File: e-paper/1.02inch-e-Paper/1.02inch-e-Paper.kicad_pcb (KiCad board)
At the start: 2 copper layers, 70 x 20.9 mm, 23 parts

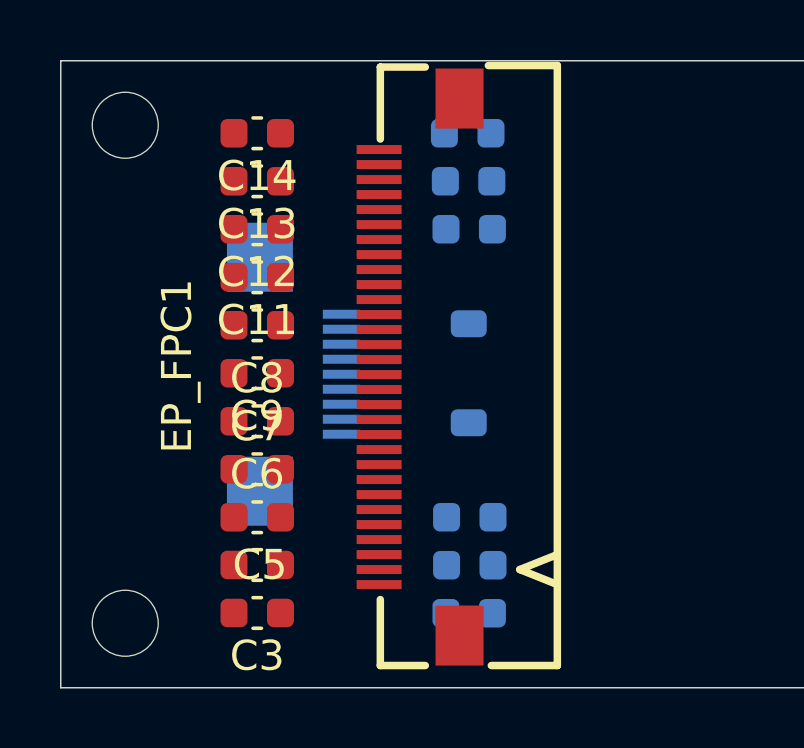
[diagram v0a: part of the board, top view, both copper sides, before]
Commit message: use 10pin connector socket instead of 9
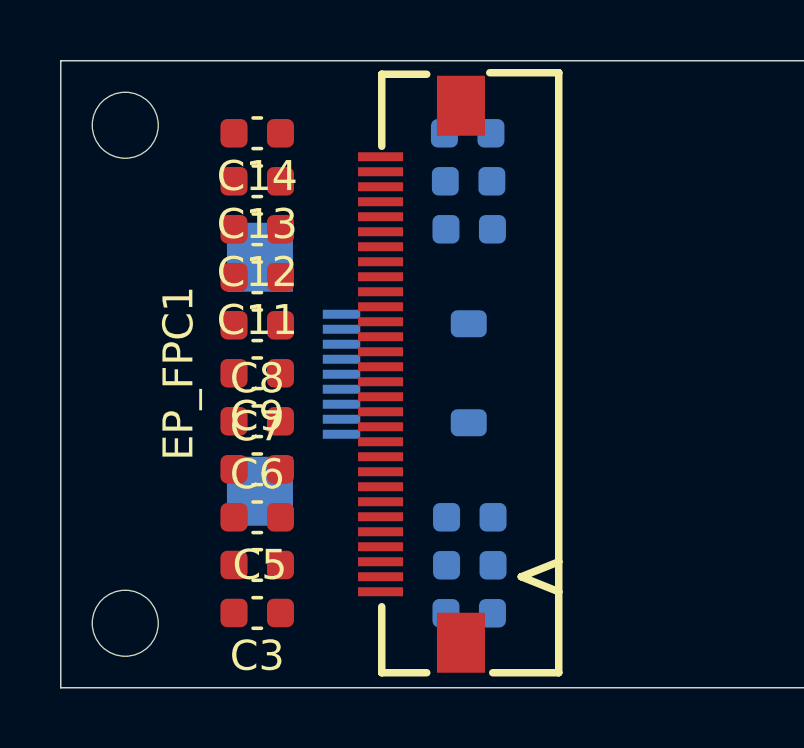
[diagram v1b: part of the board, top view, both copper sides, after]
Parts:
- moved EP_FPC1 0.24 mm to (12.0, 0.00)
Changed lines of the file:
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@@
 			)
 		)
-		(property "Datasheet" "~"
+		(property "Datasheet" ""
 			(at 0 0 0)
 			(layer "F.Fab")
@@
 			)
 		)
-		(property "Datasheet" "~"
+		(property "Datasheet" ""
 			(at 0 0 0)
 			(layer "F.Fab")
@@
 			)
 		)
-		(property "Datasheet" "~"
+		(property "Datasheet" ""
 			(at 0 0 0)
 			(layer "F.Fab")
@@
 			)
 		)
-		(property "Datasheet" "~"
+		(property "Datasheet" ""
 			(at 0 0 0)
 			(layer "F.Fab")
@@
 			)
 		)
-		(property "Datasheet" "~"
+		(property "Datasheet" ""
 			(at 0 0 0)
 			(layer "F.Fab")
@@
 			)
 		)
-		(property "Datasheet" "~"
+		(property "Datasheet" ""
 			(at 0 0 0)
 			(layer "F.Fab")
@@
 			)
 		)
-		(property "Datasheet" "~"
+		(property "Datasheet" ""
 			(at 0 0 0)
 			(layer "F.Fab")
@@
 			)
 		)
-		(property "Datasheet" "~"
+		(property "Datasheet" ""
 			(at 0 0 0)
 			(layer "F.Fab")
@@
 			)
 		)
-		(property "Datasheet" "~"
+		(property "Datasheet" ""
 			(at 0 0 0)
 			(layer "F.Fab")
@@
 	(footprint "ErgoCai.pretty:FPC-SMD_AFC01-S30FCA-00"
 		(layer "F.Cu")
-		(at 11.9525 -0.24 90)
+		(at 12 0 90)
 		(property "Reference" "EP_FPC1"
 			(at 0.0325 -8.075 90)
@@
 			)
 		)
-		(property "Datasheet" "~"
+		(property "Datasheet" ""
 			(at 0 0 0)
 			(layer "F.Fab")
@@
 			)
 		)
-		(property "Datasheet" "~"
+		(property "Datasheet" ""
 			(at 0 0 0)
 			(layer "F.Fab")
@@
 			)
 		)
-		(property "Datasheet" "~"
+		(property "Datasheet" ""
 			(at 0 0 0)
 			(layer "B.Fab")
@@
 			)
 		)
-		(property "Datasheet" "~"
+		(property "Datasheet" ""
 			(at 0 0 0)
 			(layer "B.Fab")
@@
 			)
 		)
-		(property "Datasheet" "~"
+		(property "Datasheet" ""
 			(at 0 0 270)
 			(unlocked yes)
@@
 			)
 		)
-		(property "Datasheet" "~"
+		(property "Datasheet" ""
 			(at 0 0 0)
 			(layer "B.Fab")
@@
 			)
 		)
-		(property "Datasheet" "~"
+		(property "Datasheet" ""
 			(at 0 0 0)
 			(layer "B.Fab")
@@
 			)
 		)
-		(property "Datasheet" "~"
+		(property "Datasheet" ""
 			(at 0 0 0)
 			(layer "B.Fab")
@@
 			)
 		)
-		(property "Datasheet" "~"
+		(property "Datasheet" ""
 			(at 0 0 180)
 			(layer "B.Fab")

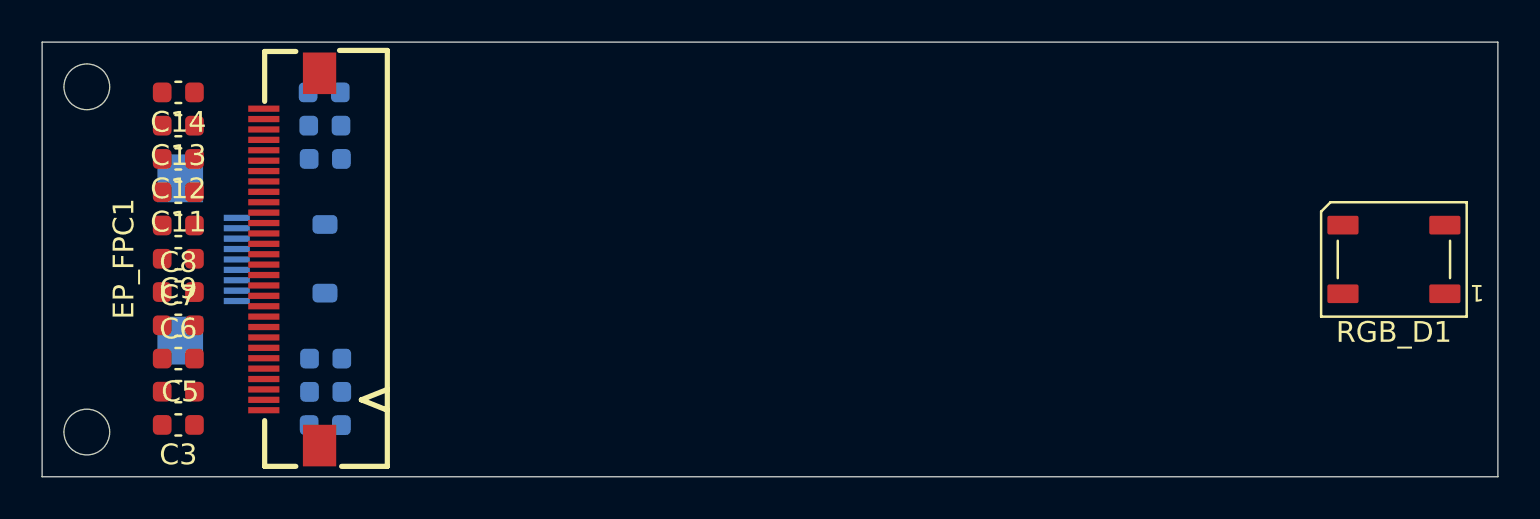
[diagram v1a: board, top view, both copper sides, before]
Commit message: updat e-paper module
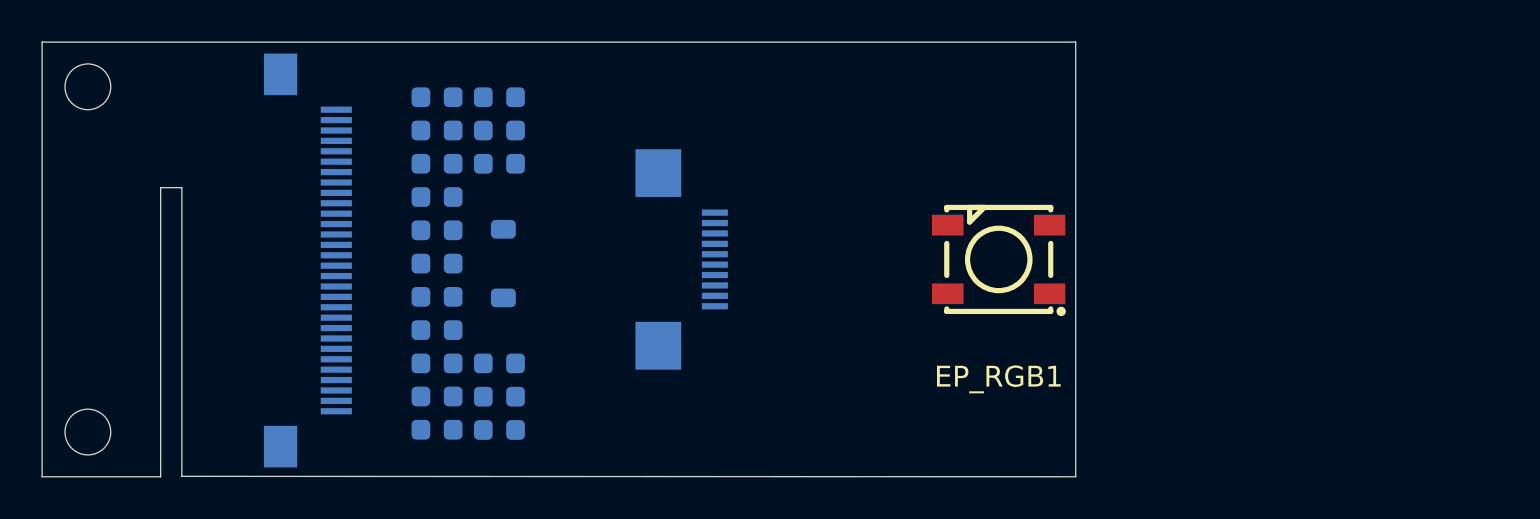
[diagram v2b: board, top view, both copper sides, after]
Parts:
- C10, C11, C12, C13, C14, C3, C5, C6, C7, C8, C9, EP_FPC1: moved to B.Cu
- EP_FPC2: value AFD01-S09FCA-00 -> AFD01-S10FCA-00; footprint ErgoCai.pretty:FPC-SMD_9P-P0.50_JS_AFD01-S09FCA-00 -> ErgoCai.pretty:FPC-SMD_10P-P0.50_JS_AFD01-S10FCA-00
- EP_RGB1: renamed from RGB_D1; footprint ErgoCai.pretty:LED_WS2812B_PLCC4_5.0x5.0mm_P3.2mm -> ErgoCai.pretty:LED-SMD_4P-L5.0-W5.0-TL_WS2812B-B
- moved EP_FPC2 23.0 mm to (31.0, 0.00)
- moved EP_RGB1 19.0 mm to (46.0, 0.00)
- moved C10 12.4 mm to (19.0, -1.40), turned to 0 degrees
- moved C11 12.4 mm to (19.0, -3.00), turned to 0 degrees
- moved C12 12.4 mm to (19.0, -4.60), turned to 0 degrees
- moved C13 12.4 mm to (19.0, -6.20), turned to 0 degrees
- moved C14 12.4 mm to (19.0, -7.80), turned to 0 degrees
- moved C3 12.4 mm to (19.0, 8.19), turned to 0 degrees
- moved C5 12.4 mm to (19.0, 6.59), turned to 180 degrees
- moved C6 12.4 mm to (19.0, 5.00), turned to 180 degrees
- moved C7 12.4 mm to (19.0, 3.40), turned to 180 degrees
- moved C8 12.4 mm to (19.0, 1.80), turned to 180 degrees
- moved C9 12.4 mm to (19.0, 0.20), turned to 0 degrees
- moved C17 9.10 mm to (22.0, -4.60)
- moved C15 8.89 mm to (22.0, -7.80), turned to 180 degrees
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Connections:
- EP_FPC2 pad 10: GND -> unconnected-(EP_FPC2-Pad10)
- EP_FPC2 pad 2: 3.3V -> GPIO_DIN
- EP_FPC2 pad 3: EP_DIN -> EP_BUSY
- EP_FPC2 pad 4: EP_CLK -> EP_RST
- EP_FPC2 pad 5: EP_CS -> EP_DC
- EP_FPC2 pad 6: EP_DC -> EP_CS
- EP_FPC2 pad 7: EP_RST -> EP_CLK
- EP_FPC2 pad 8: EP_BUSY -> EP_DIN
- EP_FPC2 pad 9: GPIO_DIN -> 3.3V
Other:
- board size 70 x 20.9 mm -> 49.7 x 20.9 mm
